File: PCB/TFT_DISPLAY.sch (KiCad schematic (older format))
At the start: 0 parts

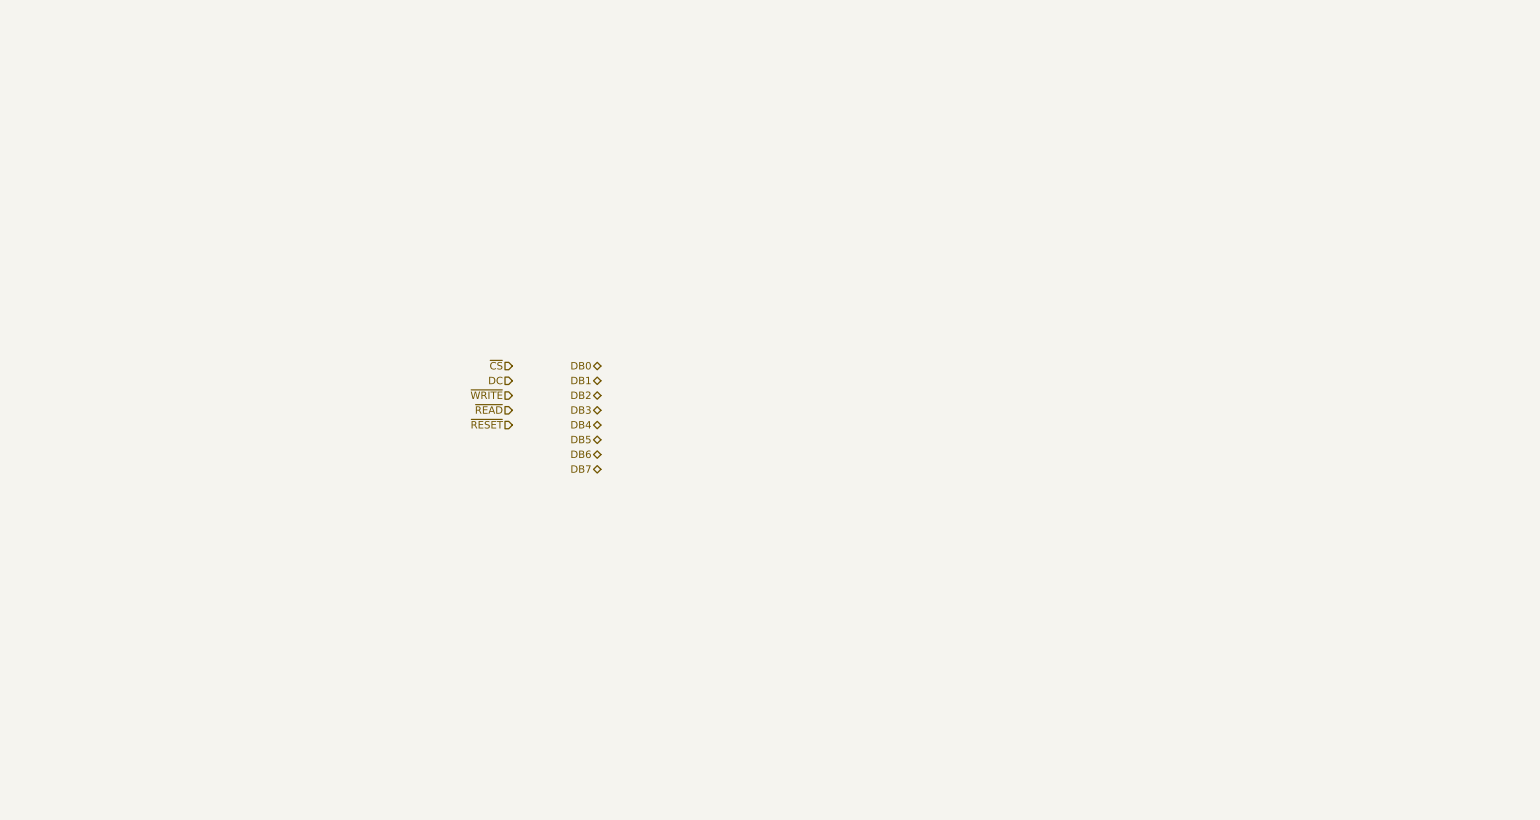
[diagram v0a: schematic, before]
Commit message: Added TFT levelshifting and connected FPC connector
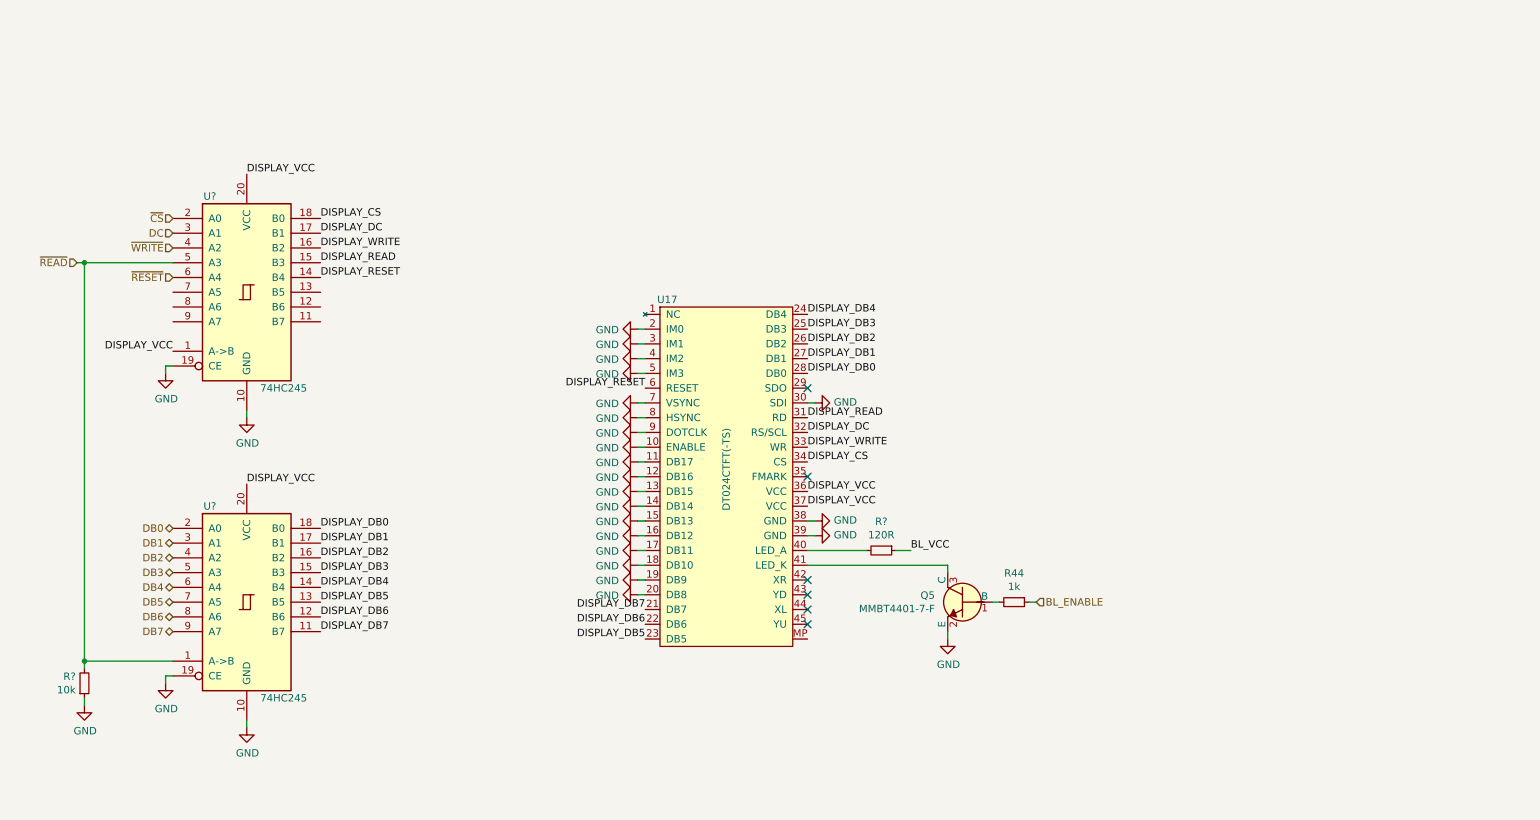
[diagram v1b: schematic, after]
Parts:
- added Q5: MMBT4401-7-F, digikey-footprints:SOT-23-3, symbol dk_Transistors-Bipolar-BJT-Single:MMBT4401-7-F
- added R44: 1k, symbol Device:R_Small
- added R?: 120R, symbol Device:R_Small
- added R?: 10k, symbol Device:R_Small
- added U17: DT024CTFT(-TS), symbol custom:DT024CTFT(-TS)
- added U? (x2): 74HC245, symbol 74xx:74HC245
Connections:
- net DB0: now also U?.2 (A0)
- net DB1: now also U?.3 (A1)
- net DB2: now also U?.4 (A2)
- net DB3: now also U?.5 (A3)
- net DB4: now also U?.6 (A4)
- net DB5: now also U?.7 (A5)
- net DB6: now also U?.8 (A6)
- net DB7: now also U?.9 (A7)
- net DC: now also U?.3 (A1)
- net ~CS: now also U?.2 (A0)
- net ~READ: now also R?.2, U?.1 (A->B), U?.5 (A3)
- net ~RESET: now also U?.6 (A4)
- net ~WRITE: now also U?.4 (A2)
- new net: R?.2, U17.40 (LED_A)
- new net: Q5.3 (C), U17.41 (LED_K)
- new net: Q5.1 (B), R44.2
- new net BL_ENABLE: R44.1
- new net BL_VCC: R?.1
- new net DISPLAY_CS: U17.34 (CS), U?.18 (B0)
- new net DISPLAY_DB0: U17.28 (DB0), U?.18 (B0)
- new net DISPLAY_DB1: U17.27 (DB1), U?.17 (B1)
- new net DISPLAY_DB2: U17.26 (DB2), U?.16 (B2)
- new net DISPLAY_DB3: U17.25 (DB3), U?.15 (B3)
- new net DISPLAY_DB4: U17.24 (DB4), U?.14 (B4)
- new net DISPLAY_DB5: U17.23 (DB5), U?.13 (B5)
- new net DISPLAY_DB6: U17.22 (DB6), U?.12 (B6)
- new net DISPLAY_DB7: U17.21 (DB7), U?.11 (B7)
- new net DISPLAY_DC: U17.32 (RS/SCL), U?.17 (B1)
- new net DISPLAY_READ: U17.31 (RD), U?.15 (B3)
- new net DISPLAY_RESET: U17.6 (RESET), U?.14 (B4)
- new net DISPLAY_VCC: U17.36 (VCC), U17.37 (VCC), U?.1 (A->B), U?.20 (VCC), U?.20 (VCC)
- new net DISPLAY_WRITE: U17.33 (WR), U?.16 (B2)
- new net GND: Q5.2 (E), R?.1, U17.10 (ENABLE), U17.11 (DB17), U17.12 (DB16), U17.13 (DB15), U17.14 (DB14), U17.15 (DB13), U17.16 (DB12), U17.17 (DB11), U17.18 (DB10), U17.19 (DB9), U17.2 (IM0), U17.20 (DB8), U17.3 (IM1), U17.30 (SDI), U17.38 (GND), U17.39 (GND), U17.4 (IM2), U17.5 (IM3), U17.7 (VSYNC), U17.8 (HSYNC), U17.9 (DOTCLK), U?.10 (GND), U?.10 (GND), U?.19 (CE), U?.19 (CE)
- no-connect marks 0 -> 6

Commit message: Renamed TFT interface pins
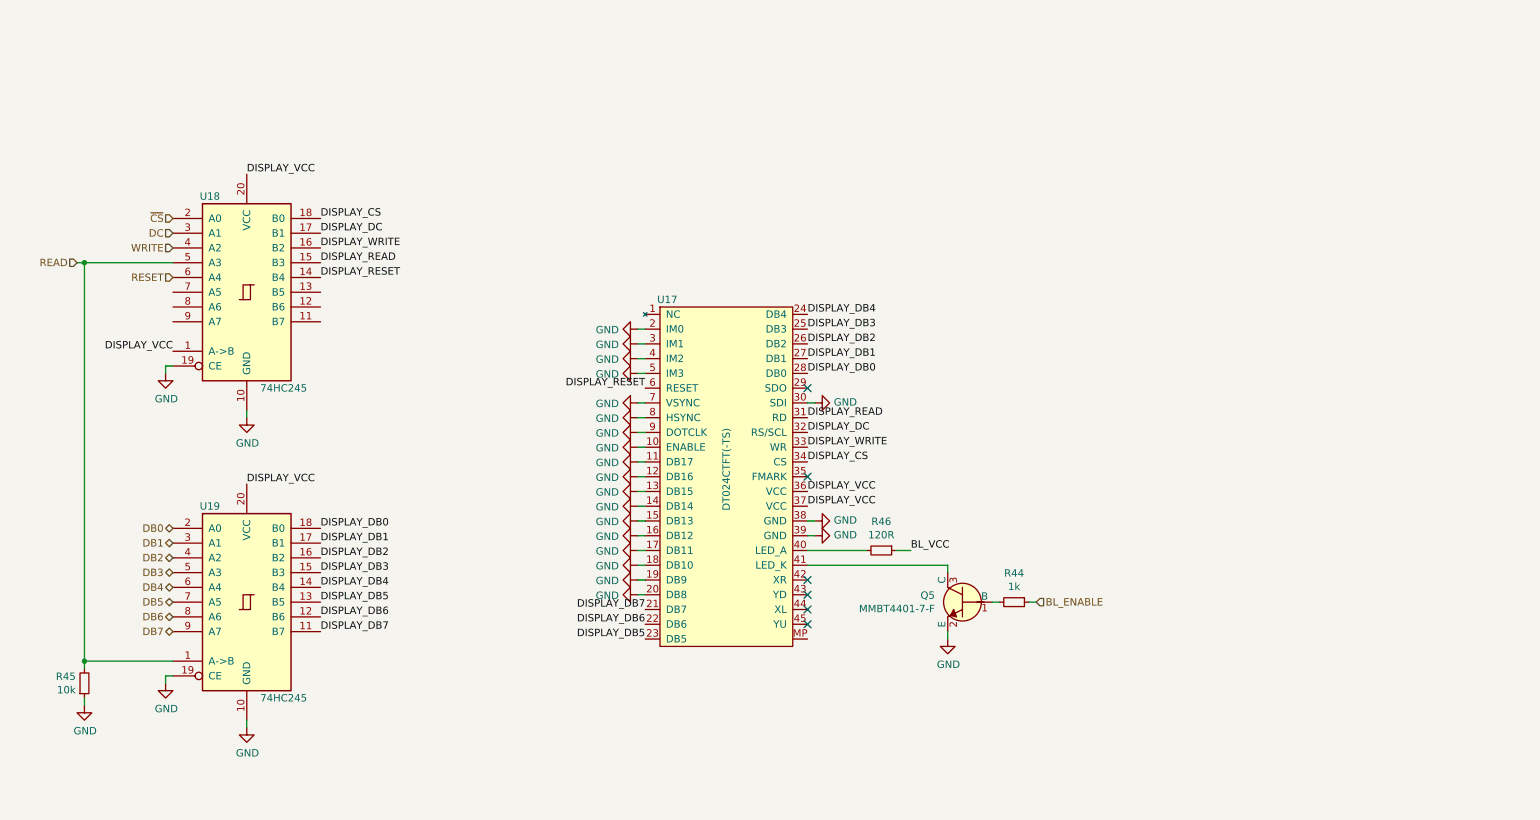
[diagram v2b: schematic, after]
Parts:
- gave numbers to parts that had none: 4
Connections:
- net ~READ renamed READ
- net ~RESET renamed RESET
- net ~WRITE renamed WRITE
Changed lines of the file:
@@
 DC
 Text HLabel 2550 2300 0    50   Input ~ 0
-~WRITE
+WRITE
 Text HLabel 1900 2400 0    50   Input ~ 0
-~READ
+READ
 Text HLabel 2550 2500 0    50   Input ~ 0
-~RESET
+RESET
 Text HLabel 2550 4900 0    50   BiDi ~ 0
 DB7
@@
 DISPLAY_DB0
 $Comp
-L Device:R_Small R?
+L Device:R_Small R46
 U 1 1 5E9E0C0E
 P 7350 4350
-F 0 "R?" V 7154 4350 50  0000 C CNN
+F 0 "R46" V 7154 4350 50  0000 C CNN
 F 1 "120R" V 7245 4350 50  0000 C CNN
 F 2 "" H 7350 4350 50  0001 C CNN
@@
 	7550 4350 7450 4350
 $Comp
-L power:GND #PWR?
+L power:GND #PWR0181
 U 1 1 5E9E5AD4
 P 6900 4250
-F 0 "#PWR?" H 6900 4000 50  0001 C CNN
+F 0 "#PWR0181" H 6900 4000 50  0001 C CNN
 F 1 "GND" V 6905 4122 50  0000 R CNN
 F 2 "" H 6900 4250 50  0001 C CNN
@@
 $EndComp
 $Comp
-L power:GND #PWR?
+L power:GND #PWR0180
 U 1 1 5E9E5E52
 P 6900 4150
-F 0 "#PWR?" H 6900 3900 50  0001 C CNN
+F 0 "#PWR0180" H 6900 3900 50  0001 C CNN
 F 1 "GND" V 6905 4022 50  0000 R CNN
 F 2 "" H 6900 4150 50  0001 C CNN
@@
 DISPLAY_VCC
 $Comp
-L 74xx:74HC245 U?
+L 74xx:74HC245 U19
 U 1 1 5E9F8F76
 P 3050 4700
-F 0 "U?" H 2800 5350 50  0000 C CNN
+F 0 "U19" H 2800 5350 50  0000 C CNN
 F 1 "74HC245" H 3300 4050 50  0000 C CNN
 F 2 "" H 3050 4700 50  0001 C CNN
@@
 $EndComp
 $Comp
-L power:GND #PWR?
+L power:GND #PWR0158
 U 1 1 5E9FC70C
 P 3050 3450
-F 0 "#PWR?" H 3050 3200 50  0001 C CNN
+F 0 "#PWR0158" H 3050 3200 50  0001 C CNN
 F 1 "GND" H 3055 3277 50  0000 C CNN
 F 2 "" H 3050 3450 50  0001 C CNN
@@
 	3050 3400 3050 3450
 $Comp
-L power:GND #PWR?
+L power:GND #PWR0160
 U 1 1 5E9FCC47
 P 3050 5550
-F 0 "#PWR?" H 3050 5300 50  0001 C CNN
+F 0 "#PWR0160" H 3050 5300 50  0001 C CNN
 F 1 "GND" H 3055 5377 50  0000 C CNN
 F 2 "" H 3050 5550 50  0001 C CNN
@@
 	3050 5500 3050 5550
 $Comp
-L 74xx:74HC245 U?
+L 74xx:74HC245 U18
 U 1 1 5E9F7E5A
 P 3050 2600
-F 0 "U?" H 2800 3250 50  0000 C CNN
+F 0 "U18" H 2800 3250 50  0000 C CNN
 F 1 "74HC245" H 3300 1950 50  0000 C CNN
 F 2 "" H 3050 2600 50  0001 C CNN
@@
 $EndComp
 $Comp
-L power:GND #PWR?
+L power:GND #PWR0156
 U 1 1 5EA06E87
 P 2500 3150
-F 0 "#PWR?" H 2500 2900 50  0001 C CNN
+F 0 "#PWR0156" H 2500 2900 50  0001 C CNN
 F 1 "GND" H 2505 2977 50  0000 C CNN
 F 2 "" H 2500 3150 50  0001 C CNN
@@
 	2500 3100 2550 3100
 $Comp
-L power:GND #PWR?
+L power:GND #PWR0157
 U 1 1 5EA07520
 P 2500 5250
-F 0 "#PWR?" H 2500 5000 50  0001 C CNN
+F 0 "#PWR0157" H 2500 5000 50  0001 C CNN
 F 1 "GND" H 2505 5077 50  0000 C CNN
 F 2 "" H 2500 5250 50  0001 C CNN
@@
 Connection ~ 1950 2400
 $Comp
-L Device:R_Small R?
+L Device:R_Small R45
 U 1 1 5EA1924F
 P 1950 5250
-F 0 "R?" H 1891 5204 50  0000 R CNN
+F 0 "R45" H 1891 5204 50  0000 R CNN
 F 1 "10k" H 1891 5295 50  0000 R CNN
 F 2 "" H 1950 5250 50  0001 C CNN
@@
 $EndComp
 $Comp
-L power:GND #PWR?
+L power:GND #PWR0155
 U 1 1 5EA1ADBC
 P 1950 5400
-F 0 "#PWR?" H 1950 5150 50  0001 C CNN
+F 0 "#PWR0155" H 1950 5150 50  0001 C CNN
 F 1 "GND" H 1955 5227 50  0000 C CNN
 F 2 "" H 1950 5400 50  0001 C CNN
@@
 BL_VCC
 $Comp
-L power:GND #PWR?
+L power:GND #PWR0165
 U 1 1 5EA4E841
 P 5700 3350
-F 0 "#PWR?" H 5700 3100 50  0001 C CNN
+F 0 "#PWR0165" H 5700 3100 50  0001 C CNN
 F 1 "GND" V 5705 3222 50  0000 R CNN
 F 2 "" H 5700 3350 50  0001 C CNN
@@
 	5700 3350 5750 3350
 $Comp
-L power:GND #PWR?
+L power:GND #PWR0166
 U 1 1 5EA50BAB
 P 5700 3450
-F 0 "#PWR?" H 5700 3200 50  0001 C CNN
+F 0 "#PWR0166" H 5700 3200 50  0001 C CNN
 F 1 "GND" V 5705 3322 50  0000 R CNN
 F 2 "" H 5700 3450 50  0001 C CNN
@@
 	5700 3450 5750 3450
 $Comp
-L power:GND #PWR?
+L power:GND #PWR0167
 U 1 1 5EA5136D
 P 5700 3550
-F 0 "#PWR?" H 5700 3300 50  0001 C CNN
+F 0 "#PWR0167" H 5700 3300 50  0001 C CNN
 F 1 "GND" V 5705 3422 50  0000 R CNN
 F 2 "" H 5700 3550 50  0001 C CNN
@@
 	5700 3550 5750 3550
 $Comp
-L power:GND #PWR?
+L power:GND #PWR0168
 U 1 1 5EA51B97
 P 5700 3650
-F 0 "#PWR?" H 5700 3400 50  0001 C CNN
+F 0 "#PWR0168" H 5700 3400 50  0001 C CNN
 F 1 "GND" V 5705 3522 50  0000 R CNN
 F 2 "" H 5700 3650 50  0001 C CNN
@@
 	5700 3650 5750 3650
 $Comp
-L power:GND #PWR?
+L power:GND #PWR0169
 U 1 1 5EA52432
 P 5700 3750
-F 0 "#PWR?" H 5700 3500 50  0001 C CNN
+F 0 "#PWR0169" H 5700 3500 50  0001 C CNN
 F 1 "GND" V 5705 3622 50  0000 R CNN
 F 2 "" H 5700 3750 50  0001 C CNN
@@
 	5700 3750 5750 3750
 $Comp
-L power:GND #PWR?
+L power:GND #PWR0170
 U 1 1 5EA52D95
 P 5700 3850
-F 0 "#PWR?" H 5700 3600 50  0001 C CNN
+F 0 "#PWR0170" H 5700 3600 50  0001 C CNN
 F 1 "GND" V 5705 3722 50  0000 R CNN
 F 2 "" H 5700 3850 50  0001 C CNN
@@
 	5700 3850 5750 3850
 $Comp
-L power:GND #PWR?
+L power:GND #PWR0171
 U 1 1 5EA5374B
 P 5700 3950
-F 0 "#PWR?" H 5700 3700 50  0001 C CNN
+F 0 "#PWR0171" H 5700 3700 50  0001 C CNN
 F 1 "GND" V 5705 3822 50  0000 R CNN
 F 2 "" H 5700 3950 50  0001 C CNN
@@
 	5700 3950 5750 3950
 $Comp
-L power:GND #PWR?
+L power:GND #PWR0172
 U 1 1 5EA5417B
 P 5700 4050
-F 0 "#PWR?" H 5700 3800 50  0001 C CNN
+F 0 "#PWR0172" H 5700 3800 50  0001 C CNN
 F 1 "GND" V 5705 3922 50  0000 R CNN
 F 2 "" H 5700 4050 50  0001 C CNN
@@
 	5700 4050 5750 4050
 $Comp
-L power:GND #PWR?
+L power:GND #PWR0173
 U 1 1 5EA54B2C
 P 5700 4150
-F 0 "#PWR?" H 5700 3900 50  0001 C CNN
+F 0 "#PWR0173" H 5700 3900 50  0001 C CNN
 F 1 "GND" V 5705 4022 50  0000 R CNN
 F 2 "" H 5700 4150 50  0001 C CNN
@@
 	5700 4150 5750 4150
 $Comp
-L power:GND #PWR?
+L power:GND #PWR0174
 U 1 1 5EA55575
 P 5700 4250
-F 0 "#PWR?" H 5700 4000 50  0001 C CNN
+F 0 "#PWR0174" H 5700 4000 50  0001 C CNN
 F 1 "GND" V 5705 4122 50  0000 R CNN
 F 2 "" H 5700 4250 50  0001 C CNN
@@
 	5700 4250 5750 4250
 $Comp
-L power:GND #PWR?
+L power:GND #PWR0175
 U 1 1 5EA56089
 P 5700 4350
-F 0 "#PWR?" H 5700 4100 50  0001 C CNN
+F 0 "#PWR0175" H 5700 4100 50  0001 C CNN
 F 1 "GND" V 5705 4222 50  0000 R CNN
 F 2 "" H 5700 4350 50  0001 C CNN
@@
 	5700 4350 5750 4350
 $Comp
-L power:GND #PWR?
+L power:GND #PWR0176
 U 1 1 5EA56BC3
 P 5700 4450
-F 0 "#PWR?" H 5700 4200 50  0001 C CNN
+F 0 "#PWR0176" H 5700 4200 50  0001 C CNN
 F 1 "GND" V 5705 4322 50  0000 R CNN
 F 2 "" H 5700 4450 50  0001 C CNN
@@
 	5700 4450 5750 4450
 $Comp
-L power:GND #PWR?
+L power:GND #PWR0177
 U 1 1 5EA57804
 P 5700 4550
-F 0 "#PWR?" H 5700 4300 50  0001 C CNN
+F 0 "#PWR0177" H 5700 4300 50  0001 C CNN
 F 1 "GND" V 5705 4422 50  0000 R CNN
 F 2 "" H 5700 4550 50  0001 C CNN
@@
 	5700 4550 5750 4550
 $Comp
-L power:GND #PWR?
+L power:GND #PWR0178
 U 1 1 5EA584EF
 P 5700 4650
-F 0 "#PWR?" H 5700 4400 50  0001 C CNN
+F 0 "#PWR0178" H 5700 4400 50  0001 C CNN
 F 1 "GND" V 5705 4522 50  0000 R CNN
 F 2 "" H 5700 4650 50  0001 C CNN
@@
 	5700 4650 5750 4650
 $Comp
-L power:GND #PWR?
+L power:GND #PWR0161
 U 1 1 5EA5B670
 P 5700 2850
-F 0 "#PWR?" H 5700 2600 50  0001 C CNN
+F 0 "#PWR0161" H 5700 2600 50  0001 C CNN
 F 1 "GND" V 5705 2722 50  0000 R CNN
 F 2 "" H 5700 2850 50  0001 C CNN
@@
 	5700 2850 5750 2850
 $Comp
-L power:GND #PWR?
+L power:GND #PWR0162
 U 1 1 5EA5C075
 P 5700 2950
-F 0 "#PWR?" H 5700 2700 50  0001 C CNN
+F 0 "#PWR0162" H 5700 2700 50  0001 C CNN
 F 1 "GND" V 5705 2822 50  0000 R CNN
 F 2 "" H 5700 2950 50  0001 C CNN
@@
 	5700 2950 5750 2950
 $Comp
-L power:GND #PWR?
+L power:GND #PWR0163
 U 1 1 5EA5CB84
 P 5700 3050
-F 0 "#PWR?" H 5700 2800 50  0001 C CNN
+F 0 "#PWR0163" H 5700 2800 50  0001 C CNN
 F 1 "GND" V 5705 2922 50  0000 R CNN
 F 2 "" H 5700 3050 50  0001 C CNN
@@
 	5700 3050 5750 3050
 $Comp
-L power:GND #PWR?
+L power:GND #PWR0164
 U 1 1 5EA5D77C
 P 5700 3150
-F 0 "#PWR?" H 5700 2900 50  0001 C CNN
+F 0 "#PWR0164" H 5700 2900 50  0001 C CNN
 F 1 "GND" V 5705 3022 50  0000 R CNN
 F 2 "" H 5700 3150 50  0001 C CNN
@@
 	5700 3150 5750 3150
 $Comp
-L power:GND #PWR?
+L power:GND #PWR0179
 U 1 1 5EA60D8C
 P 6900 3350
-F 0 "#PWR?" H 6900 3100 50  0001 C CNN
+F 0 "#PWR0179" H 6900 3100 50  0001 C CNN
 F 1 "GND" V 6905 3222 50  0000 R CNN
 F 2 "" H 6900 3350 50  0001 C CNN
